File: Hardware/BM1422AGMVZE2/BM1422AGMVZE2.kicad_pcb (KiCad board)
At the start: 2 copper layers, 23.1 x 20.8 mm, 8 parts

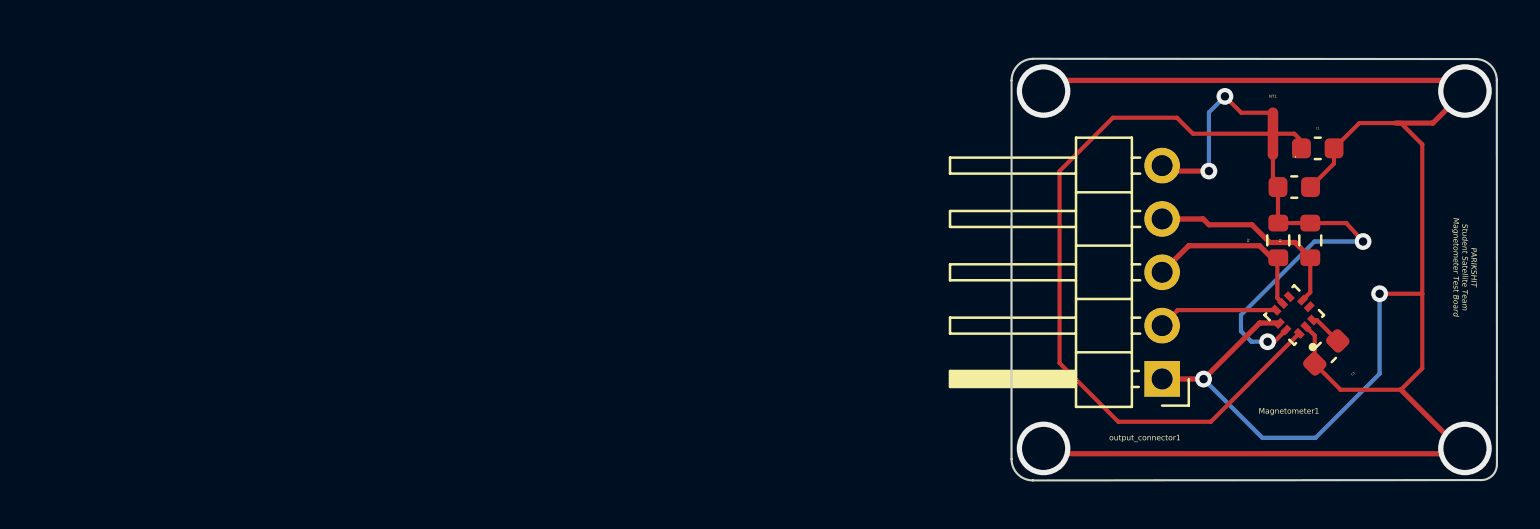
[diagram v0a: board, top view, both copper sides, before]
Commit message: GND via has exposed copper now
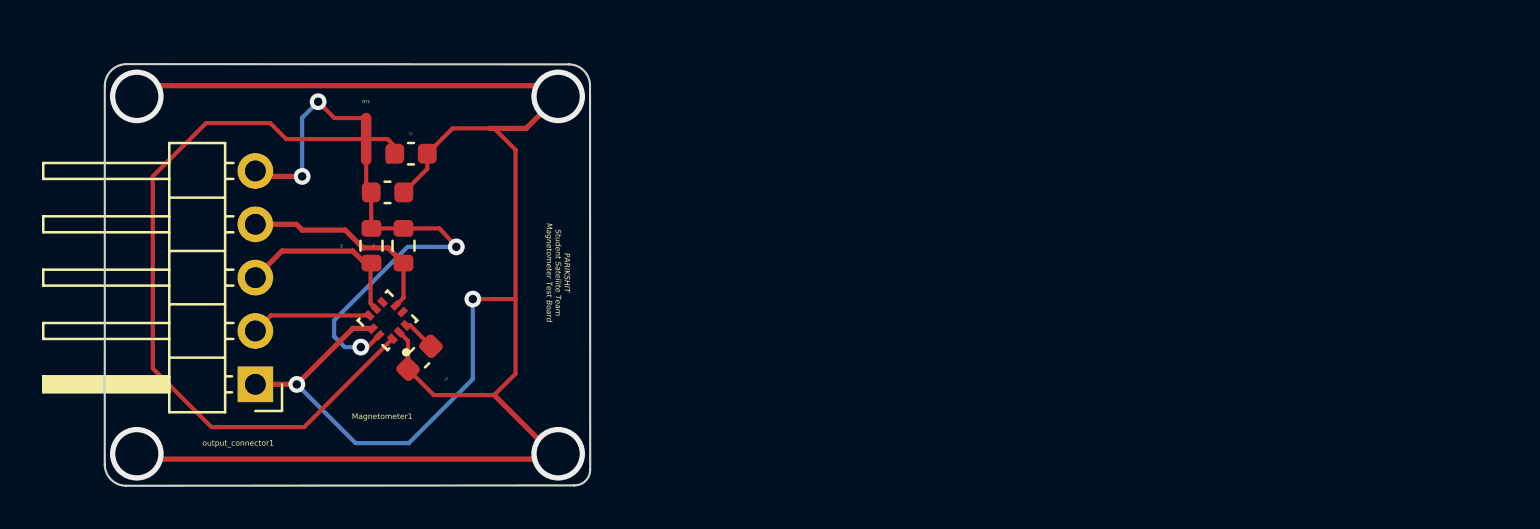
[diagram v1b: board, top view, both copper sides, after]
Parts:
- moved C1 43.2 mm to (150.7, 97.0)
- moved C2 43.2 mm to (149.6, 98.8)
- moved C3 43.2 mm to (151.1, 106.7)
- moved Magnetometer1 43.2 mm to (149.6, 104.9)
- moved NT1 43.2 mm to (148.6, 96.3)
- moved R1 43.2 mm to (150.4, 101.3)
- moved R2 43.2 mm to (148.8, 101.3)
- moved output_connector1 43.2 mm to (143.3, 107.9)
